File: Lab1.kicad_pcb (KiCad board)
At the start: 2 copper layers, 60 x 40 mm, 49 parts, among them J1 USB_OTG, J2 SWD, SW2 Reset, U1 PMW3389, U2 AP2125N-3.3TRG, U3 MIC5235YM5-TR, U4 STM32F411RETx, U5 USBLC6-2SC6, Y1 16Mhz

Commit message: Backup of working 1st prototype
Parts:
- moved C7 1.08 mm to (74.4, 53.9)
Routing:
- net Net-(R2-Pad2): track 0.00 -> 24.8 mm, vias 0 -> 5
- net NCS: track 33.7 -> 41.9 mm
- net +3V3: track 162.8 -> 158.7 mm
- net SCK: track 41.5 -> 45.5 mm, vias 2 -> 3
- net MOSI: track 65.8 -> 68.1 mm
- net Net-(C7-Pad1): track 2.82 -> 4.79 mm
- net Motion: track 42.7 -> 43.7 mm
- net +5V: track 78.5 -> 79.5 mm
- net GND: track 300.7 -> 301.1 mm, vias 14 -> 16
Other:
- outline, holes or cut-outs redrawn

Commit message: 2nd design, quite happy with this one!
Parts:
- removed the R5 at (61.7, 59.1)
- removed the R5 at (61.7, 63.0)
- removed the R6 at (66.4, 59.0)
- removed the R6 at (66.4, 63.0)
- added R5: 820, Resistor_SMD:R_0815_2038Metric_Pad1.20x4.05mm_HandSolder, F.Cu at (81.6, 32.1)
- added R6: 47, Resistor_SMD:R_0815_2038Metric_Pad1.20x4.05mm_HandSolder, F.Cu at (54.9, 66.2)
- moved U2 51.2 mm to (53.5, 35.6), turned to 0 degrees
- moved C5 49.5 mm to (101.1, 34.0), turned to 180 degrees
- moved J1 47.7 mm to (46.2, 48.2), turned to 270 degrees
- moved TP1 46.3 mm to (66.4, 59.2)
- moved C1 45.6 mm to (58.4, 52.2), turned to 180 degrees
- moved C6 44.7 mm to (95.1, 34.0)
- moved C20 44.3 mm to (63.6, 32.1)
- moved Y1 40.5 mm to (98.1, 37.1), turned to 180 degrees
- moved C15 40.4 mm to (94.4, 63.9), turned to 0 degrees
- moved U3 39.2 mm to (51.1, 61.9)
- moved R3 38.9 mm to (47.1, 66.2)
- moved U5 38.8 mm to (53.5, 50.1), turned to 0 degrees
- moved TP2 38.5 mm to (54.2, 56.3)
- moved TP3 38.4 mm to (100.5, 31.7), turned to 90 degrees
- moved C19 37.5 mm to (76.1, 32.1)
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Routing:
- net SWO: track 45.1 -> 9.73 mm, vias 1 -> 0
- net +5V: track 79.5 -> 47.7 mm
- net BOOT0: track 89.0 -> 58.9 mm, vias 2 -> 5
- net MOSI: track 68.1 -> 38.8 mm, vias 1 -> 0
- net VDD: track 64.2 -> 35.8 mm
- net OUT_D-: track 13.3 -> 40.8 mm
- net SWCLK: track 38.7 -> 11.8 mm, vias 2 -> 0
- net GND: track 301.1 -> 274.9 mm, vias 16 -> 18
- net SCK: track 45.5 -> 21.2 mm, vias 3 -> 2
- net Motion: track 43.7 -> 19.8 mm, vias 1 -> 2
- net OUT_D+: track 15.8 -> 39.6 mm
- net SWDIO: track 39.2 -> 15.7 mm
- net NCS: track 41.9 -> 18.6 mm
- net MISO: track 61.2 -> 41.5 mm, vias 2 -> 0
- net Net-(R2-Pad2): track 24.8 -> 5.17 mm, vias 5 -> 0
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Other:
- outline, holes or cut-outs redrawn

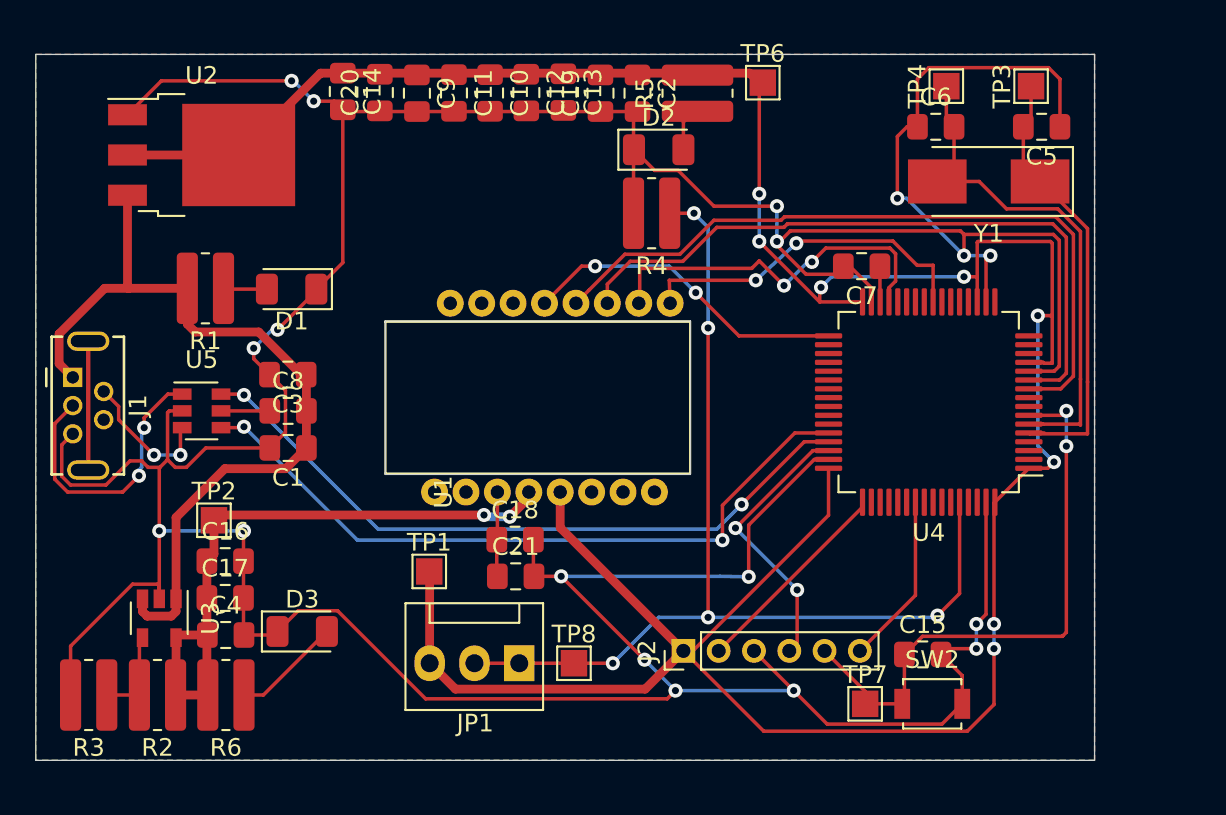
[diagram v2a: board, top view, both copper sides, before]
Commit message: Fixed decoupling capacitors
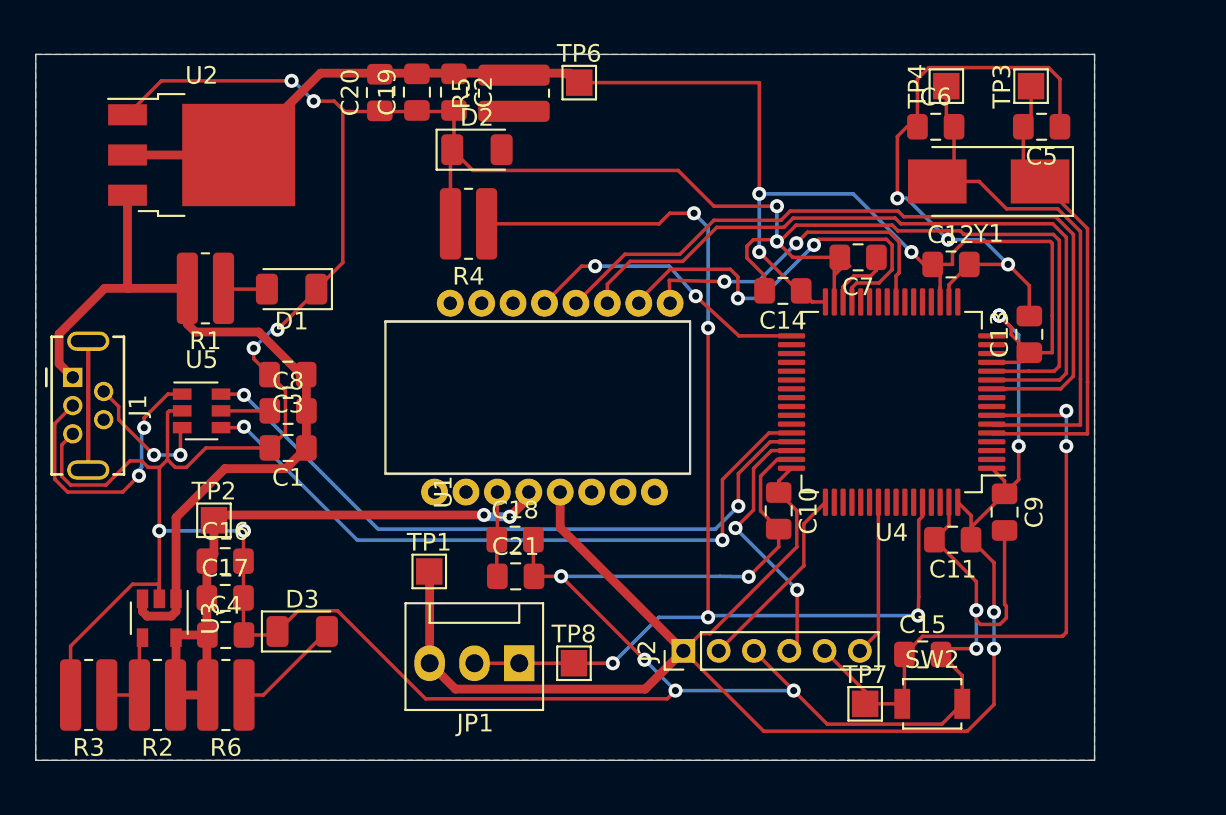
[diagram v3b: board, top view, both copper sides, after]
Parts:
- moved C9 40.9 mm to (99.0, 55.8)
- moved C11 37.9 mm to (96.1, 57.4), turned to 180 degrees
- moved C13 29.8 mm to (100.4, 45.8), turned to 90 degrees
- moved C10 28.8 mm to (86.2, 55.8)
- moved C14 27.4 mm to (86.4, 43.3), turned to 180 degrees
- moved C12 26.0 mm to (96.0, 41.8), turned to 0 degrees
- moved C2 10.4 mm to (67.8, 32.0)
- moved C19 10.4 mm to (65.7, 32.0)
- moved R5 10.4 mm to (71.2, 32.1)
- moved TP6 10.4 mm to (74.9, 31.5)
- moved R4 10.4 mm to (68.6, 39.5)
- moved D2 10.3 mm to (69.1, 35.3)
- moved U4 2.10 mm to (92.6, 49.6)
- moved C7 0.54 mm to (90.7, 41.4)
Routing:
- net GND: track 274.9 -> 297.8 mm
- net +3V3: track 172.5 -> 185.2 mm
- net BOOT0: track 58.9 -> 68.0 mm
- net Net-(D2-Pad2): track 2.42 -> 0.00 mm
- net MOSI: track 38.8 -> 41.2 mm
- net MISO: track 41.5 -> 43.9 mm
- net NRST: track 33.4 -> 35.5 mm
- net NCS: track 18.6 -> 16.5 mm
- net SCK: track 21.2 -> 23.2 mm
- net Net-(C7-Pad1): track 2.03 -> 3.87 mm
- net Net-(C6-Pad2): track 30.0 -> 31.3 mm
- net OUT_D-: track 40.8 -> 39.5 mm
- net Net-(C5-Pad2): track 26.0 -> 27.3 mm
- net OUT_D+: track 39.6 -> 38.6 mm
- net SWO: track 9.73 -> 8.86 mm
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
